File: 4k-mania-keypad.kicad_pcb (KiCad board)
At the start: 2 copper layers, 112 x 45 mm, 47 parts, among them J1 USB_C_Receptacle_USB2.0, J2 Pico Ezmate, J3 Pico Ezmate, J4 Pico Ezmate, J5 Pico Ezmate, SW1 EC11E18244A5, SW2 EC11E18244A5, SW3 MX_SW_HS, SW4 MX_SW_HS, SW5 MX_SW_HS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

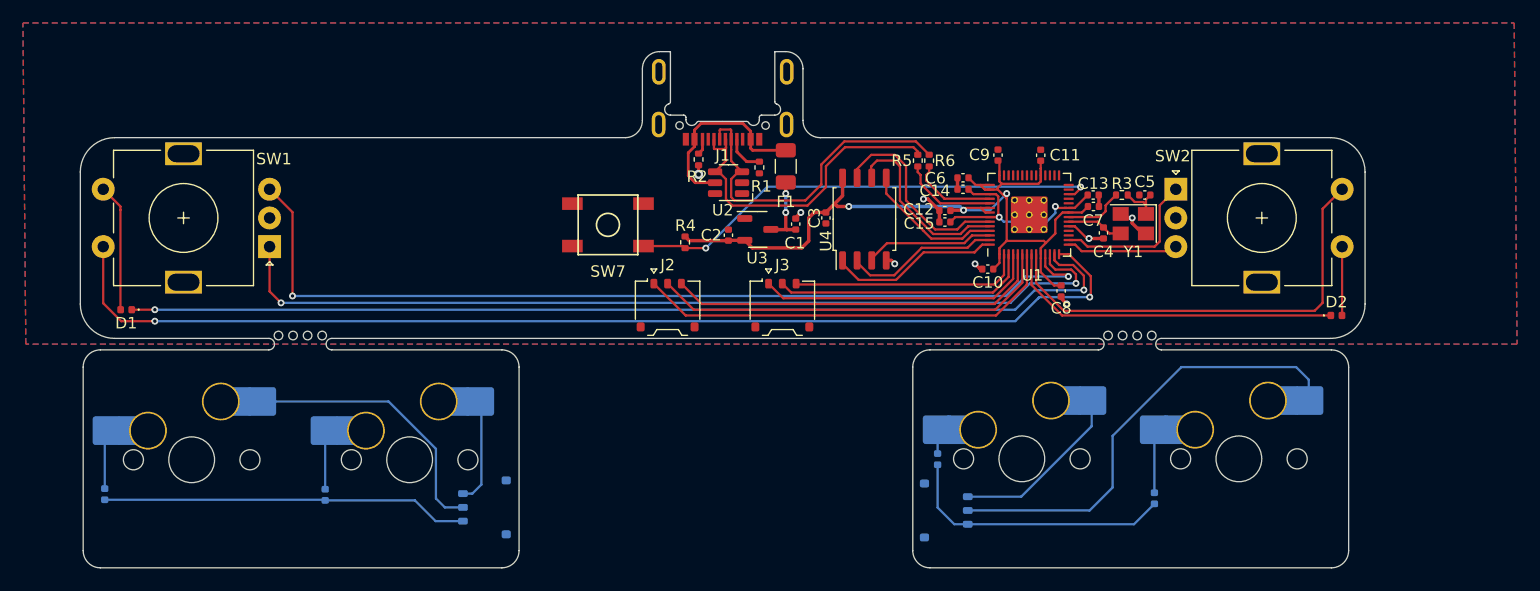
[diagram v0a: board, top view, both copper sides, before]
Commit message: Improved usb power section layout
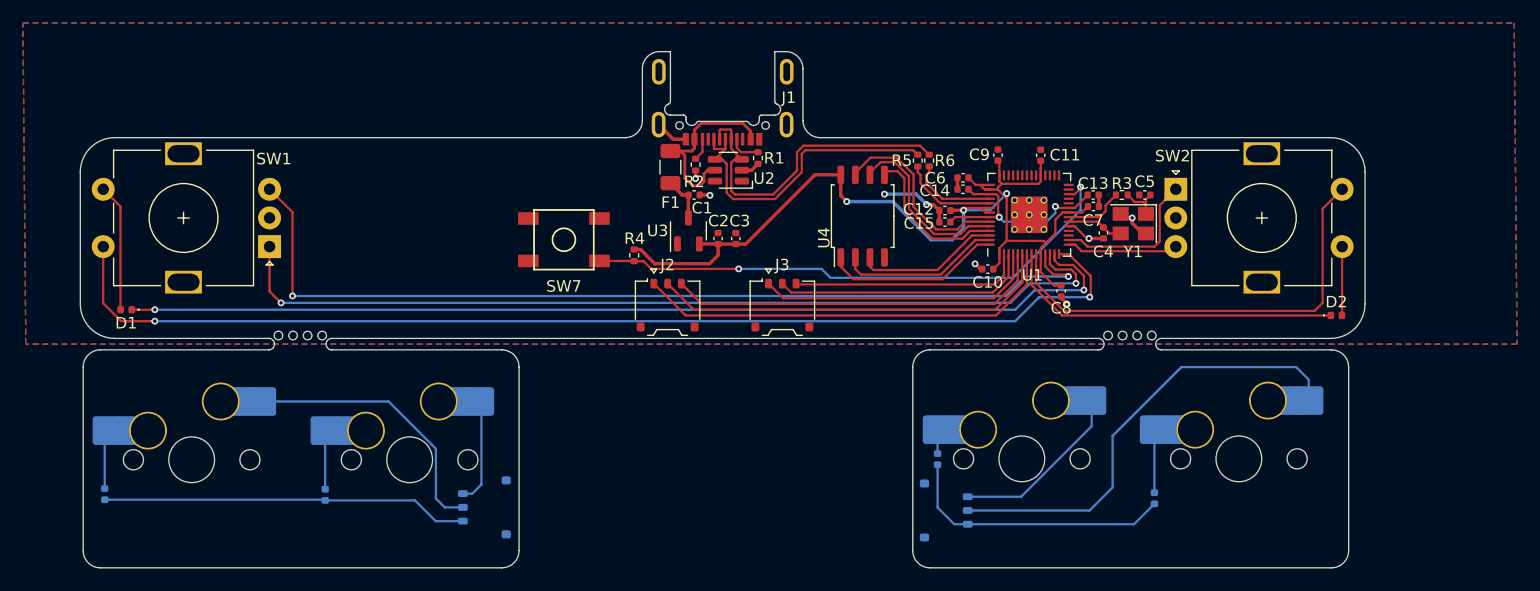
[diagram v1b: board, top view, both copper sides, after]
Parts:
- moved F1 10.1 mm to (146.4, 82.6)
- moved C1 9.21 mm to (148.5, 85.0), turned to 0 degrees
- moved C3 8.06 mm to (152.1, 88.8), turned to 90 degrees
- moved U3 6.05 mm to (148.0, 88.1), turned to 90 degrees
- moved R4 4.58 mm to (143.3, 90.3)
- moved SW7 4.05 mm to (137.2, 88.9)
- moved U2 1.08 mm to (151.5, 82.8)
- moved C2 0.95 mm to (150.6, 88.8)
- moved R1 0.83 mm to (154.1, 81.8)
- moved R2 0.52 mm to (148.6, 82.4)
- moved U4 0.30 mm to (163.2, 86.8)
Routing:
- net +3.3V: track 73.2 -> 83.0 mm
- net GND: track 15.9 -> 23.3 mm
- net /reset: track 41.8 -> 48.4 mm
- net +5V: track 6.20 -> 4.01 mm, vias 2 -> 0
- net /USB_D+: track 28.8 -> 27.4 mm
- net /SD0: track 12.3 -> 13.7 mm
- net /SD2: track 11.3 -> 12.6 mm
- net /USB_D-: track 29.7 -> 28.7 mm
- net /CLK: track 16.2 -> 15.5 mm
- net /SD1: track 13.5 -> 14.2 mm
- net Net-(J1-CC1): track 3.41 -> 2.75 mm
- net /SD3: track 17.6 -> 17.0 mm
- net Net-(J1-CC2): track 1.39 -> 1.95 mm
